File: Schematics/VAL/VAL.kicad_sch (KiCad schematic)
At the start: 2 parts

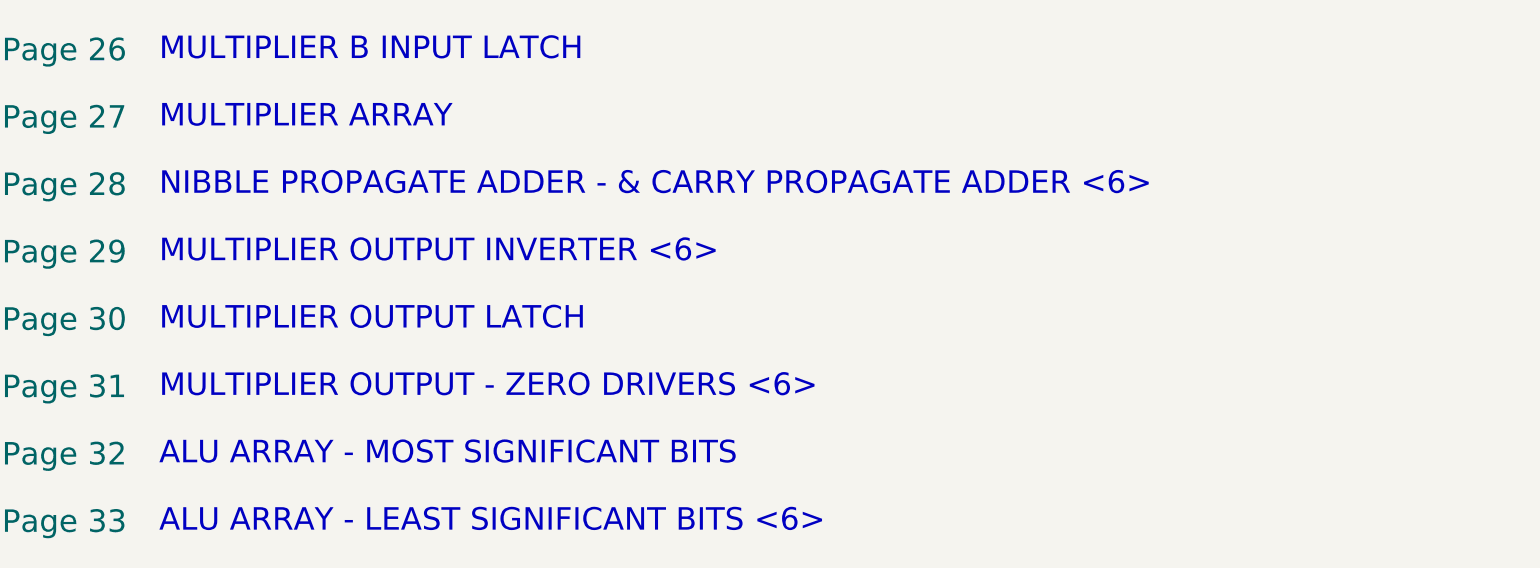
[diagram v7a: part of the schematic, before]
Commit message: Megacomp multiplier latches
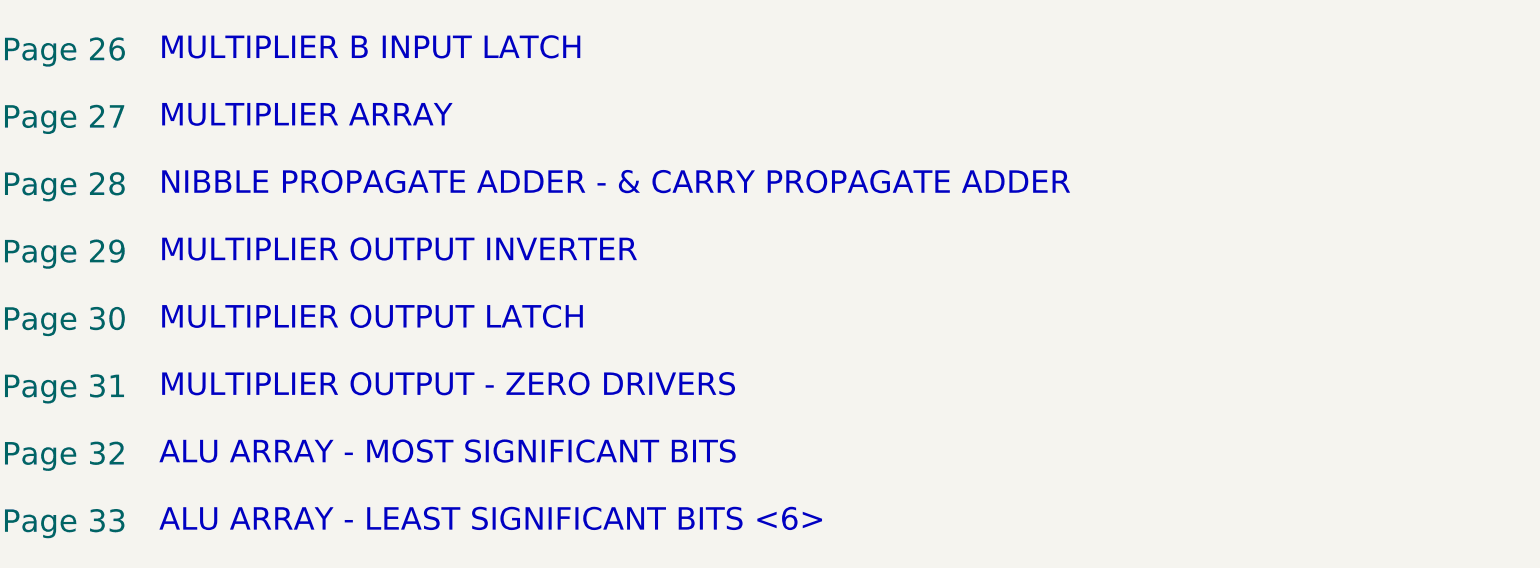
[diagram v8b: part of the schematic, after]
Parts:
- U101, U102: value (none) -> ~
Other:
- note added: "MULTIPLIER OUTPUT - ZERO DRIVERS"
- note added: "MULTIPLIER OUTPUT INVERTER"
- note added: "NIBBLE PROPAGATE ADDER - & CARRY PROPAGATE ADDER"
- note removed: "MULTIPLIER OUTPUT - ZERO DRIVERS <6>"
- note removed: "MULTIPLIER OUTPUT INVERTER <6>"
- note removed: "NIBBLE PROPAGATE ADDER - & CARRY PROPAGATE ADDER <6>"
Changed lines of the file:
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@@
   (wire (pts (xy 566.42 241.3) (xy 566.42 243.84) ) (stroke (width 0) (type default) ) )
   (wire (pts (xy 566.42 259.08) (xy 566.42 261.62) ) (stroke (width 0) (type default) ) )
-  (symbol (lib_id "r1000:PU") (at 566.42 241.3 0) (unit 1) (in_bom yes) (on_board yes) (property "Reference" "#PWR0102" (id 0) (at 566.42 241.3 0) (effects (font (size 1.27 1.27) ) hide ) ) (property "Value" "" (id 1) (at 566.42 241.3 0) (effects (font (size 1.27 1.27) ) hide ) ) (property "Footprint" "" (id 2) (at 566.42 241.3 0) (effects (font (size 1.27 1.27) ) hide ) ) (property "Datasheet" "" (id 3) (at 566.42 241.3 0) (effects (font (size 1.27 1.27) ) hide ) ) (pin "1" ) )
-  (symbol (lib_id "r1000:Pull_Down") (at 566.42 259.08 0) (unit 1) (in_bom yes) (on_board yes) (property "Reference" "U102" (id 0) (at 566.42 259.08 0) (effects (font (size 1.27 1.27) ) ) ) (property "Value" "" (id 1) (at 566.42 255.27 0) (effects (font (size 2.54 2.54) ) ) ) (property "Footprint" "" (id 2) (at 566.42 259.08 0) (effects (font (size 1.27 1.27) ) hide ) ) (property "Datasheet" "" (id 3) (at 566.42 259.08 0) (effects (font (size 1.27 1.27) ) hide ) ) (pin "1" ) )
-  (symbol (lib_id "r1000:Pull_Up") (at 566.42 243.84 0) (unit 1) (in_bom yes) (on_board yes) (property "Reference" "U101" (id 0) (at 566.42 243.84 0) (effects (font (size 1.27 1.27) ) ) ) (property "Value" "" (id 1) (at 566.42 247.65 0) (effects (font (size 2.54 2.54) ) ) ) (property "Footprint" "" (id 2) (at 566.42 243.84 0) (effects (font (size 1.27 1.27) ) hide ) ) (property "Datasheet" "" (id 3) (at 566.42 243.84 0) (effects (font (size 1.27 1.27) ) hide ) ) (pin "1" ) )
-  (symbol (lib_id "r1000:PD") (at 566.42 261.62 0) (unit 1) (in_bom no) (on_board yes) (property "Reference" "#PWR0101" (id 0) (at 566.42 261.62 0) (effects (font (size 1.27 1.27) ) hide ) ) (property "Value" "" (id 1) (at 566.42 261.62 0) (effects (font (size 1.27 1.27) ) hide ) ) (property "Footprint" "" (id 2) (at 566.42 261.62 0) (effects (font (size 1.27 1.27) ) hide ) ) (property "Datasheet" "" (id 3) (at 566.42 261.62 0) (effects (font (size 1.27 1.27) ) hide ) ) (pin "1" ) )
+  (symbol (lib_id "r1000:PU") (at 566.42 241.3 0) (unit 1) (in_bom yes) (on_board yes) (property "Reference" "#PWR0102" (id 0) (at 566.42 241.3 0) (effects (font (size 1.27 1.27) ) hide ) ) (property "Value" "~" (id 1) (at 566.42 241.3 0) (effects (font (size 1.27 1.27) ) hide ) ) (property "Footprint" "" (id 2) (at 566.42 241.3 0) (effects (font (size 1.27 1.27) ) hide ) ) (property "Datasheet" "" (id 3) (at 566.42 241.3 0) (effects (font (size 1.27 1.27) ) hide ) ) (pin "1" ) )
+  (symbol (lib_id "r1000:Pull_Down") (at 566.42 259.08 0) (unit 1) (in_bom yes) (on_board yes) (property "Reference" "U102" (id 0) (at 566.42 259.08 0) (effects (font (size 1.27 1.27) ) ) ) (property "Value" "~" (id 1) (at 566.42 255.27 0) (effects (font (size 2.54 2.54) ) ) ) (property "Footprint" "" (id 2) (at 566.42 259.08 0) (effects (font (size 1.27 1.27) ) hide ) ) (property "Datasheet" "" (id 3) (at 566.42 259.08 0) (effects (font (size 1.27 1.27) ) hide ) ) (pin "1" ) )
+  (symbol (lib_id "r1000:Pull_Up") (at 566.42 243.84 0) (unit 1) (in_bom yes) (on_board yes) (property "Reference" "U101" (id 0) (at 566.42 243.84 0) (effects (font (size 1.27 1.27) ) ) ) (property "Value" "~" (id 1) (at 566.42 247.65 0) (effects (font (size 2.54 2.54) ) ) ) (property "Footprint" "" (id 2) (at 566.42 243.84 0) (effects (font (size 1.27 1.27) ) hide ) ) (property "Datasheet" "" (id 3) (at 566.42 243.84 0) (effects (font (size 1.27 1.27) ) hide ) ) (pin "1" ) )
+  (symbol (lib_id "r1000:PD") (at 566.42 261.62 0) (unit 1) (in_bom no) (on_board yes) (property "Reference" "#PWR0101" (id 0) (at 566.42 261.62 0) (effects (font (size 1.27 1.27) ) hide ) ) (property "Value" "~" (id 1) (at 566.42 261.62 0) (effects (font (size 1.27 1.27) ) hide ) ) (property "Footprint" "" (id 2) (at 566.42 261.62 0) (effects (font (size 1.27 1.27) ) hide ) ) (property "Datasheet" "" (id 3) (at 566.42 261.62 0) (effects (font (size 1.27 1.27) ) hide ) ) (pin "1" ) )
   (text "Board: VAL Branch: megacomp2" (at 7.62 370.84 0) (effects (font (size 7.62 7.62) (thickness 1.27) bold ) (justify left bottom) ) )
   (sheet_instances
@@
   (sheet (at 12.70 218.44) (size 20.32 5.08) (property "Sheet name" "Page 27" (id 0) (at 35.56 223.52 0) (effects (font (size 2.54 2.54) ) (justify left bottom) ) ) (property "Sheet file" "pg_27.kicad_sch" (id 1) (at 35.56 220.98 0) (effects (justify left bottom) hide ) ) )
   (text "MULTIPLIER ARRAY" (at 53.34 223.52 0) (effects (font (size 2.54 2.54) ) (justify left bottom) ) )
-  (sheet (at 12.70 226.06) (size 20.32 5.08) (property "Sheet name" "Page 28" (id 0) (at 35.56 231.14 0) (effects (font (size 2.54 2.54) ) (justify left bottom) ) ) (property "Sheet file" "pg_28.kicad_sch" (id 1) (at 35.56 228.60 0) (effects (justify left bottom) hide ) ) (fill (color 192 192 192 1.0) ) )
-  (text "NIBBLE PROPAGATE ADDER - & CARRY PROPAGATE ADDER <6>" (at 53.34 231.14 0) (effects (font (size 2.54 2.54) ) (justify left bottom) ) )
-  (sheet (at 12.70 233.68) (size 20.32 5.08) (property "Sheet name" "Page 29" (id 0) (at 35.56 238.76 0) (effects (font (size 2.54 2.54) ) (justify left bottom) ) ) (property "Sheet file" "pg_29.kicad_sch" (id 1) (at 35.56 236.22 0) (effects (justify left bottom) hide ) ) (fill (color 192 192 192 1.0) ) )
-  (text "MULTIPLIER OUTPUT INVERTER <6>" (at 53.34 238.76 0) (effects (font (size 2.54 2.54) ) (justify left bottom) ) )
+  (sheet (at 12.70 226.06) (size 20.32 5.08) (property "Sheet name" "Page 28" (id 0) (at 35.56 231.14 0) (effects (font (size 2.54 2.54) ) (justify left bottom) ) ) (property "Sheet file" "pg_28.kicad_sch" (id 1) (at 35.56 228.60 0) (effects (justify left bottom) hide ) ) )
+  (text "NIBBLE PROPAGATE ADDER - & CARRY PROPAGATE ADDER" (at 53.34 231.14 0) (effects (font (size 2.54 2.54) ) (justify left bottom) ) )
+  (sheet (at 12.70 233.68) (size 20.32 5.08) (property "Sheet name" "Page 29" (id 0) (at 35.56 238.76 0) (effects (font (size 2.54 2.54) ) (justify left bottom) ) ) (property "Sheet file" "pg_29.kicad_sch" (id 1) (at 35.56 236.22 0) (effects (justify left bottom) hide ) ) )
+  (text "MULTIPLIER OUTPUT INVERTER" (at 53.34 238.76 0) (effects (font (size 2.54 2.54) ) (justify left bottom) ) )
   (sheet (at 12.70 241.30) (size 20.32 5.08) (property "Sheet name" "Page 30" (id 0) (at 35.56 246.38 0) (effects (font (size 2.54 2.54) ) (justify left bottom) ) ) (property "Sheet file" "pg_30.kicad_sch" (id 1) (at 35.56 243.84 0) (effects (justify left bottom) hide ) ) )
   (text "MULTIPLIER OUTPUT LATCH" (at 53.34 246.38 0) (effects (font (size 2.54 2.54) ) (justify left bottom) ) )
-  (sheet (at 12.70 248.92) (size 20.32 5.08) (property "Sheet name" "Page 31" (id 0) (at 35.56 254.00 0) (effects (font (size 2.54 2.54) ) (justify left bottom) ) ) (property "Sheet file" "pg_31.kicad_sch" (id 1) (at 35.56 251.46 0) (effects (justify left bottom) hide ) ) (fill (color 192 192 192 1.0) ) )
-  (text "MULTIPLIER OUTPUT - ZERO DRIVERS <6>" (at 53.34 254.00 0) (effects (font (size 2.54 2.54) ) (justify left bottom) ) )
+  (sheet (at 12.70 248.92) (size 20.32 5.08) (property "Sheet name" "Page 31" (id 0) (at 35.56 254.00 0) (effects (font (size 2.54 2.54) ) (justify left bottom) ) ) (property "Sheet file" "pg_31.kicad_sch" (id 1) (at 35.56 251.46 0) (effects (justify left bottom) hide ) ) )
+  (text "MULTIPLIER OUTPUT - ZERO DRIVERS" (at 53.34 254.00 0) (effects (font (size 2.54 2.54) ) (justify left bottom) ) )
   (sheet (at 12.70 256.54) (size 20.32 5.08) (property "Sheet name" "Page 32" (id 0) (at 35.56 261.62 0) (effects (font (size 2.54 2.54) ) (justify left bottom) ) ) (property "Sheet file" "pg_32.kicad_sch" (id 1) (at 35.56 259.08 0) (effects (justify left bottom) hide ) ) )
   (text "ALU ARRAY - MOST SIGNIFICANT BITS" (at 53.34 261.62 0) (effects (font (size 2.54 2.54) ) (justify left bottom) ) )
